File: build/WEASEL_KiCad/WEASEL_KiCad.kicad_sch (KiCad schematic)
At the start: 1 part

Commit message: Virtual Patch bay added to schematic
Virtual modular patch bay added
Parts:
- added D1, D10, D11, D12, D13, D14, D15, D16, D17, D18, D19, D2, D20, D21, D22, D23, D24, D25, D26, D27, D28, D29, D3, D4, D6, D7, D8, D9: 1N4148, DIYSynthMNL:D_4148_BigPads, symbol PCM_4ms_Diode:D_Generic
- added R1, R2, R3, R4: 10k, PCM_4ms_Resistor:R_Axial_DIN0207_L6.3mm_D2.5mm_P7.62mm_Horizontal, symbol Device:R
- added SW1: SEQ>PULSER, symbol Switch:SW_Push
- added SW10: RANDOMVOLT>MODOSC_FREQ, symbol Switch:SW_Push
- added SW11: SEQ>MODOSC_MODAMNT, symbol Switch:SW_Push
- added SW12: EG>MODOSC_MODAMNT, symbol Switch:SW_Push
- added SW13: PULSER>MODOSC_MODAMNT, symbol Switch:SW_Push
- added SW14: RANDOMVOLT>MODOSC_MODAMNT, symbol Switch:SW_Push
- added SW15: SEQ>COMPLEX_PITCH, symbol Switch:SW_Push
- added SW16: EG>COMPLEX_PITCH, symbol Switch:SW_Push
- added SW17: PULSER>COMPLEX_PITCH, symbol Switch:SW_Push
- added SW18: RANDOMVOLT>COMPLEX_PITCH, symbol Switch:SW_Push
- added SW19: SEQ>COMPLEX_TIMBRE, symbol Switch:SW_Push
- added SW2: SW_SPDT_MSM, symbol Switch:SW_SPDT_MSM
- added SW20: EG>COMPLEX_TIMBRE, symbol Switch:SW_Push
- added SW21: PULSER>COMPLEX_TIMBRE, symbol Switch:SW_Push
- added SW22: RANDOMVOLT>COMPLEX_TIMBRE, symbol Switch:SW_Push
- added SW23: SEQ>LPG_LEVEL1, symbol Switch:SW_Push
- added SW24: EG>LPG_LEVEL1, symbol Switch:SW_Push
- added SW25: PULSER>LPG_LEVEL1, symbol Switch:SW_Push
- added SW26: RANDOMVOLT>LPG_LEVEL1, symbol Switch:SW_Push
- added SW27: SEQ>LPG_LEVEL2, symbol Switch:SW_Push
- added SW28: EG>LPG_LEVEL2, symbol Switch:SW_Push
- added SW29: PULSER>LPG_LEVEL2, symbol Switch:SW_Push
- added SW3: EG>PULSER, symbol Switch:SW_Push
- added SW30: RANDOMVOLT>LPG_LEVEL2, symbol Switch:SW_Push
- added SW4: N/C, symbol Switch:SW_Push
- added SW5: RNDMVOLT>PULSER, symbol Switch:SW_Push
- added SW7: SEQ>MODOSC_FREQ, symbol Switch:SW_Push
- added SW8: EG>MODOSC_FREQ, symbol Switch:SW_Push
- added SW9: PULSER>MODOSC_FREQ, symbol Switch:SW_Push
- added U1: CD74HC4067M, Package_SO:SOIC-24W_7.5x15.4mm_P1.27mm, symbol 74xx:CD74HC4067M
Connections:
- net Vcc: now reaches A1.38 (3V3_D)
- net Vcc: now also U1.24 (VCC)
- net DGND: now reaches A1.40 (DGND)
- net DGND: now also R1.2, R2.2, R3.2, R4.2, U1.12 (GND), U1.15 (~{E})
- new net: D25.2 (A), SW26.2
- new net: D17.2 (A), SW18.2
- new net: D23.2 (A), SW24.2
- new net: D7.2 (A), SW8.2
- new net: D27.2 (A), SW28.2
- new net: D26.2 (A), SW27.2
- new net: D6.2 (A), SW7.2
- new net: D16.2 (A), SW17.2
- new net: D11.2 (A), SW12.2
- new net: D20.2 (A), SW21.2
- new net: D12.2 (A), SW13.2
- new net: D9.2 (A), SW10.2
- new net: D1.2 (A), SW1.2
- new net: D8.2 (A), SW9.2
- new net: D22.2 (A), SW23.2
- new net: D24.2 (A), SW25.2
- new net: D4.2 (A), SW5.2
- new net: D19.2 (A), SW20.2
- new net: D13.2 (A), SW14.2
- new net: D10.2 (A), SW11.2
- new net: D14.2 (A), SW15.2
- new net: D28.2 (A), SW29.2
- new net: D15.2 (A), SW16.2
- new net: D21.2 (A), SW22.2
- new net: D18.2 (A), SW19.2
- new net: D29.2 (A), SW30.2
- new net: D2.2 (A), SW3.2
- new net: D3.2 (A), SW4.2
- new net X0: R1.1, SW1.1, SW11.1, SW15.1, SW19.1, SW23.1, SW27.1, SW7.1
- new net X1: R2.1, SW12.1, SW16.1, SW20.1, SW24.1, SW28.1, SW3.1, SW8.1
- new net X2: R3.1, SW13.1, SW17.1, SW21.1, SW25.1, SW29.1, SW4.1, SW9.1
- new net X3: R4.1, SW10.1, SW14.1, SW18.1, SW22.1, SW26.1, SW30.1, SW5.1
- new net Y0: D1.1 (K), D2.1 (K), D3.1 (K), D4.1 (K)
- new net Y1: D6.1 (K), D7.1 (K), D8.1 (K), D9.1 (K)
- new net Y2: D10.1 (K), D11.1 (K), D12.1 (K), D13.1 (K)
- new net Y3: D14.1 (K), D15.1 (K), D16.1 (K), D17.1 (K)
- new net Y4: D18.1 (K), D19.1 (K), D20.1 (K), D21.1 (K)
- new net Y5: D22.1 (K), D23.1 (K), D24.1 (K), D25.1 (K)
- new net Y6: D26.1 (K), D27.1 (K), D28.1 (K), D29.1 (K)
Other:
- note added: "COMPLEX OSC PITCH_INPUT"
- note added: "COMPLEX OSC TIMBRE_INPUT"
- note added: "CONTROL SWITCHES"
- note added: "EG_OUTPUT"
- note added: "LPG LEVEL 1_INPUT"
- note added: "LPG LEVEL 2_INPUT"
- note added: "MOD OSC FREQ_INPUT"
- note added: "MOD OSC MOD AMNT_INPUT"
- note added: "PULSER PERIOD_INPUT"
- note added: "PULSER_OUTPUT"
- note added: "RANDOM VOLTAGE_OUTPUT"
- note added: "SEQUENCER"
- note added: "SEQUENCER_OUTPUT"
- note added: "VIRTUAL MODULAR MATRIX"

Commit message: Schematic and PCB Changes
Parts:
- removed D10, D11, D12, D13, D14, D15, D16, D17, D18, D19, D20, D21, D22, D23, D24, D25, D26, D27, D28, D29, D9: 1N4148, DIYSynthMNL:D_4148_BigPads, symbol PCM_4ms_Diode:D_Generic
- removed SW1: SEQ>PULSER, symbol Switch:SW_Push
- removed SW10: RANDOMVOLT>MODOSC_FREQ, symbol Switch:SW_Push
- removed SW11: SEQ>MODOSC_MODAMNT, symbol Switch:SW_Push
- removed SW12: EG>MODOSC_MODAMNT, symbol Switch:SW_Push
- removed SW13: PULSER>MODOSC_MODAMNT, symbol Switch:SW_Push
- removed SW14: RANDOMVOLT>MODOSC_MODAMNT, symbol Switch:SW_Push
- removed SW15: SEQ>COMPLEX_PITCH, symbol Switch:SW_Push
- removed SW16: EG>COMPLEX_PITCH, symbol Switch:SW_Push
- removed SW17: PULSER>COMPLEX_PITCH, symbol Switch:SW_Push
- removed SW18: RANDOMVOLT>COMPLEX_PITCH, symbol Switch:SW_Push
- removed SW19: SEQ>COMPLEX_TIMBRE, symbol Switch:SW_Push
- removed SW2: SW_SPDT_MSM, symbol Switch:SW_SPDT_MSM
- removed SW20: EG>COMPLEX_TIMBRE, symbol Switch:SW_Push
- removed SW21: PULSER>COMPLEX_TIMBRE, symbol Switch:SW_Push
- removed SW22: RANDOMVOLT>COMPLEX_TIMBRE, symbol Switch:SW_Push
- removed SW23: SEQ>LPG_LEVEL1, symbol Switch:SW_Push
- removed SW24: EG>LPG_LEVEL1, symbol Switch:SW_Push
- removed SW25: PULSER>LPG_LEVEL1, symbol Switch:SW_Push
- removed SW26: RANDOMVOLT>LPG_LEVEL1, symbol Switch:SW_Push
- removed SW27: SEQ>LPG_LEVEL2, symbol Switch:SW_Push
- removed SW28: EG>LPG_LEVEL2, symbol Switch:SW_Push
- removed SW29: PULSER>LPG_LEVEL2, symbol Switch:SW_Push
- removed SW3: EG>PULSER, symbol Switch:SW_Push
- removed SW30: RANDOMVOLT>LPG_LEVEL2, symbol Switch:SW_Push
- removed SW4: N/C, symbol Switch:SW_Push
- removed SW5: RNDMVOLT>PULSER, symbol Switch:SW_Push
- removed SW7: SEQ>MODOSC_FREQ, symbol Switch:SW_Push
- removed SW8: EG>MODOSC_FREQ, symbol Switch:SW_Push
- removed SW9: PULSER>MODOSC_FREQ, symbol Switch:SW_Push
- added C1, C10, C11, C12, C13, C14, C15, C16, C17, C18, C19, C2, C20, C21, C22, C23, C24, C25, C26, C3, C4, C5, C6, C7, C8, C9: 10nF, DIYSynthMNL:C_Rect_L7.0mm_W2.0mm_P5.00mm_BigPads, symbol Device:C
- added D30, D31, D32, D33, D34, D35, D36, D37, D38, D39, D40, D41, D42, D43, D44, D45, D46, D47, D48, D49, D5: 1N4148, DIYSynthMNL:D_4148_BigPads, symbol PCM_4ms_Diode:D_Generic
- added J1: MIDI IN, Connector_Audio:Jack_3.5mm_CUI_SJ1-3523N_Horizontal, symbol Connector_Audio:AudioJack3
- added J10: LPG_LEVEL2CTRL, Connector_Audio:Jack_3.5mm_QingPu_WQP-PJ398SM_Vertical_CircularHoles, symbol Connector_Audio:AudioJack2_SwitchT
- added J14: SEQ_OUTPUT2, Connector_Audio:Jack_3.5mm_QingPu_WQP-PJ398SM_Vertical_CircularHoles, symbol Connector_Audio:AudioJack2_SwitchT
- added J15: SEQ_OUTPUT3, Connector_Audio:Jack_3.5mm_QingPu_WQP-PJ398SM_Vertical_CircularHoles, symbol Connector_Audio:AudioJack2_SwitchT
- added J16: EG_OUTPUT1, Connector_Audio:Jack_3.5mm_QingPu_WQP-PJ398SM_Vertical_CircularHoles, symbol Connector_Audio:AudioJack2_SwitchT
- added J17: EG_OUTPUT2, Connector_Audio:Jack_3.5mm_QingPu_WQP-PJ398SM_Vertical_CircularHoles, symbol Connector_Audio:AudioJack2_SwitchT
- added J18: EG_OUTPUT3, Connector_Audio:Jack_3.5mm_QingPu_WQP-PJ398SM_Vertical_CircularHoles, symbol Connector_Audio:AudioJack2_SwitchT
- added J19: PLSR_OUTPUT1, Connector_Audio:Jack_3.5mm_QingPu_WQP-PJ398SM_Vertical_CircularHoles, symbol Connector_Audio:AudioJack2_SwitchT
- added J2: STEREO_OUTPUT, Connector_Audio:Jack_3.5mm_CUI_SJ1-3523N_Horizontal, symbol Connector_Audio:AudioJack3
- added J20: PLSR_OUTPUT2, Connector_Audio:Jack_3.5mm_QingPu_WQP-PJ398SM_Vertical_CircularHoles, symbol Connector_Audio:AudioJack2_SwitchT
- added J21: PLSR_OUTPUT3, Connector_Audio:Jack_3.5mm_QingPu_WQP-PJ398SM_Vertical_CircularHoles, symbol Connector_Audio:AudioJack2_SwitchT
- added J22: RNDM_OUTPUT1, Connector_Audio:Jack_3.5mm_QingPu_WQP-PJ398SM_Vertical_CircularHoles, symbol Connector_Audio:AudioJack2_SwitchT
- added J23: RNDM_OUTPUT2, Connector_Audio:Jack_3.5mm_QingPu_WQP-PJ398SM_Vertical_CircularHoles, symbol Connector_Audio:AudioJack2_SwitchT
- added J24: RNDM_OUTPUT3, Connector_Audio:Jack_3.5mm_QingPu_WQP-PJ398SM_Vertical_CircularHoles, symbol Connector_Audio:AudioJack2_SwitchT
- added J3: SEQ_OUTPUT1, Connector_Audio:Jack_3.5mm_QingPu_WQP-PJ398SM_Vertical_CircularHoles, symbol Connector_Audio:AudioJack2_SwitchT
- added J4: PLSR_PERIODCTRL, Connector_Audio:Jack_3.5mm_QingPu_WQP-PJ398SM_Vertical_CircularHoles, symbol Connector_Audio:AudioJack2_SwitchT
- added J5: MODOSC_FREQCTRL, Connector_Audio:Jack_3.5mm_QingPu_WQP-PJ398SM_Vertical_CircularHoles, symbol Connector_Audio:AudioJack2_SwitchT
- added J6: MODOSC_MODCTRL, Connector_Audio:Jack_3.5mm_QingPu_WQP-PJ398SM_Vertical_CircularHoles, symbol Connector_Audio:AudioJack2_SwitchT
- added J7: COMPOSC_PITCHCTRL, Connector_Audio:Jack_3.5mm_QingPu_WQP-PJ398SM_Vertical_CircularHoles, symbol Connector_Audio:AudioJack2_SwitchT
- added J8: COMPOSC_WAVEFOLDERCTRL, Connector_Audio:Jack_3.5mm_QingPu_WQP-PJ398SM_Vertical_CircularHoles, symbol Connector_Audio:AudioJack2_SwitchT
- added J9: LPG_LEVEL1CTRL, Connector_Audio:Jack_3.5mm_QingPu_WQP-PJ398SM_Vertical_CircularHoles, symbol Connector_Audio:AudioJack2_SwitchT
- added R10, R9: 220R, PCM_4ms_Resistor:R_Axial_DIN0207_L6.3mm_D2.5mm_P7.62mm_Horizontal, symbol Device:R
- added R5, R6, R7, R8: 10k, PCM_4ms_Resistor:R_Axial_DIN0207_L6.3mm_D2.5mm_P7.62mm_Horizontal, symbol Device:R
- added RV1: SQ_Step1, DIYSynthMNL:Potentiometer_RV09_BigPads, symbol Device:R_Potentiometer
- added RV10: PLSR_PERIOD, DIYSynthMNL:Potentiometer_RV09_BigPads, symbol Device:R_Potentiometer
- added RV11: MODOSC_FREQCTRL, DIYSynthMNL:Potentiometer_RV09_BigPads, symbol Device:R_Potentiometer
- added RV12: MODOSC_FREQ, DIYSynthMNL:Potentiometer_RV09_BigPads, symbol Device:R_Potentiometer
- added RV13: MODOSC_MODULATIONCTRL, DIYSynthMNL:Potentiometer_RV09_BigPads, symbol Device:R_Potentiometer
- added RV14: MODOSC_MODULATION, DIYSynthMNL:Potentiometer_RV09_BigPads, symbol Device:R_Potentiometer
- added RV15: MODOSC_FINE, DIYSynthMNL:Potentiometer_RV09_BigPads, symbol Device:R_Potentiometer
- added RV16: COMPLEXOSC_FREQCTRL, DIYSynthMNL:Potentiometer_RV09_BigPads, symbol Device:R_Potentiometer
- added RV17: COMPLEXOSC_FREQ, DIYSynthMNL:Potentiometer_RV09_BigPads, symbol Device:R_Potentiometer
- added RV18: COMPLEXOSC_FINE, DIYSynthMNL:Potentiometer_RV09_BigPads, symbol Device:R_Potentiometer
- added RV19: COMPLEXOSC_WAVEFOLDERCTRL, DIYSynthMNL:Potentiometer_RV09_BigPads, symbol Device:R_Potentiometer
- added RV2: SQ_Step2, DIYSynthMNL:Potentiometer_RV09_BigPads, symbol Device:R_Potentiometer
- added RV20: COMPLEXOSC_WAVEFOLDER, DIYSynthMNL:Potentiometer_RV09_BigPads, symbol Device:R_Potentiometer
- added RV21: COMPLEXOSC_TIMBRE, DIYSynthMNL:Potentiometer_RV09_BigPads, symbol Device:R_Potentiometer
- added RV22: LPG_LEVEL1CTRL, DIYSynthMNL:Potentiometer_RV09_BigPads, symbol Device:R_Potentiometer
- added RV23: LPG_LEVEL1, DIYSynthMNL:Potentiometer_RV09_BigPads, symbol Device:R_Potentiometer
- added RV24: LPG_LEVEL2CTRL, DIYSynthMNL:Potentiometer_RV09_BigPads, symbol Device:R_Potentiometer
- added RV25: LPG_LEVEL2, DIYSynthMNL:Potentiometer_RV09_BigPads, symbol Device:R_Potentiometer
- added RV26: CLOCK, DIYSynthMNL:Potentiometer_RV09_BigPads, symbol Device:R_Potentiometer
- added RV3: SQ_Step3, DIYSynthMNL:Potentiometer_RV09_BigPads, symbol Device:R_Potentiometer
- added RV4: SQ_Step4, DIYSynthMNL:Potentiometer_RV09_BigPads, symbol Device:R_Potentiometer
- added RV5: SQ_Step5, DIYSynthMNL:Potentiometer_RV09_BigPads, symbol Device:R_Potentiometer
- added RV6: EG_ATTACK, DIYSynthMNL:Potentiometer_RV09_BigPads, symbol Device:R_Potentiometer
- added RV7: EG_SUSTAIN, DIYSynthMNL:Potentiometer_RV09_BigPads, symbol Device:R_Potentiometer
- added RV8: EG_DECAY, DIYSynthMNL:Potentiometer_RV09_BigPads, symbol Device:R_Potentiometer
- added RV9: PLSR_PERIODCTRL, DIYSynthMNL:Potentiometer_RV09_BigPads, symbol Device:R_Potentiometer
- added SW1: SQ_TOGGLESTEP1, DIYSynthMNL:ToggleSwitch_MTS-102_SPDT, symbol Switch:SW_SPDT
- added SW2: SEQ_TRIGGERSELECT, PCM_4ms_Experimental_FP:SW_PUSH_6mm_H13mm, symbol Switch:SW_Push
- added SW3: SQ_TOGGLESTEP2, DIYSynthMNL:ToggleSwitch_MTS-102_SPDT, symbol Switch:SW_SPDT
- added SW31: EG_TRIGGERSELECT, PCM_4ms_Experimental_FP:SW_PUSH_6mm_H13mm, symbol Switch:SW_Push
- added SW32: EG_MODESELECT, PCM_4ms_Experimental_FP:SW_PUSH_6mm_H13mm, symbol Switch:SW_Push
- added SW33: PLSR_TRIGGERSELECT, PCM_4ms_Experimental_FP:SW_PUSH_6mm_H13mm, symbol Switch:SW_Push
- added SW34: PLSR_MODE, PCM_4ms_Experimental_FP:SW_PUSH_6mm_H13mm, symbol Switch:SW_Push
- added SW35: MODOSC_MIDITOGGLE, PCM_4ms_Experimental_FP:SW_PUSH_6mm_H13mm, symbol Switch:SW_Push
- added SW36: MODOSC_PITCHTRANGE, PCM_4ms_Experimental_FP:SW_PUSH_6mm_H13mm, symbol Switch:SW_Push
- added SW37: COMPLEXOSC_MIDITOGGLE, PCM_4ms_Experimental_FP:SW_PUSH_6mm_H13mm, symbol Switch:SW_Push
- added SW38: COMPLEXOSC_POLARITY, PCM_4ms_Experimental_FP:SW_PUSH_6mm_H13mm, symbol Switch:SW_Push
- added SW39: COMPLEXOSC_WAVETOGGLE, PCM_4ms_Experimental_FP:SW_PUSH_6mm_H13mm, symbol Switch:SW_Push
- added SW4: SQ_TOGGLESTEP3, DIYSynthMNL:ToggleSwitch_MTS-102_SPDT, symbol Switch:SW_SPDT
- added SW40: LPG_GATE1MODE, PCM_4ms_Experimental_FP:SW_PUSH_6mm_H13mm, symbol Switch:SW_Push
- added SW41: LPG_GATE2MODE, PCM_4ms_Experimental_FP:SW_PUSH_6mm_H13mm, symbol Switch:SW_Push
- added SW42: RNDMVOLTAGE_TRIGGERSELECT, PCM_4ms_Experimental_FP:SW_PUSH_6mm_H13mm, symbol Switch:SW_Push
- added SW43: CLOCK_SYNCTOGGLE, PCM_4ms_Experimental_FP:SW_PUSH_6mm_H13mm, symbol Switch:SW_Push
- added SW5: SQ_TOGGLESTEP4, DIYSynthMNL:ToggleSwitch_MTS-102_SPDT, symbol Switch:SW_SPDT
- added SW6: SEQ_STAGES, PCM_4ms_Experimental_FP:SW_PUSH_6mm_H13mm, symbol Switch:SW_Push
- added SW7: SQ_TOGGLESTEP5, DIYSynthMNL:ToggleSwitch_MTS-102_SPDT, symbol Switch:SW_SPDT
- added U2: CD74HC4067M, Package_SO:SOIC-24W_7.5x15.4mm_P1.27mm, symbol 74xx:CD74HC4067M
- added U3: 6N138, DIYSynthMNL:DIP-8_W7.62mm_LongPads, symbol Isolator:6N138
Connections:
- net DGND: now also U2.15 (~{E}); no longer A1.40 (DGND), R1.2, R2.2, R3.2, R4.2, U1.12 (GND)
- net Vcc: now also R9.1, RV1.3, RV10.3, RV11.3, RV12.3, RV13.3, RV14.3, RV15.3, RV16.3, RV17.3, RV18.3, RV19.3, RV2.3, RV20.3, RV21.3, RV22.3, RV23.3, RV24.3, RV25.3, RV26.3, RV3.3, RV4.3, RV5.3, RV6.3, RV7.3, RV8.3, RV9.3, U2.24 (VCC), U3.8 (VCC)
- net X0: now also A1.13 (I2C1_SDA), SW2.1, SW3.2 (B), SW33.1, SW37.1, SW41.1
- net X1: now also A1.14 (USART1_TX), SW34.1, SW38.1, SW4.2 (B), SW42.1, SW6.1
- net X2: now also A1.24 (ADC_2), SW31.1, SW35.1, SW39.1, SW43.1, SW5.2 (B)
- net X3: now also A1.25 (ADC_3), SW1.2 (B), SW32.1, SW36.1, SW40.1, SW7.2 (B)
- net Y0: now also A1.9 (SPI1_SCK), D30.1 (K), D31.1 (K), D32.1 (K), D5.1 (K); no longer D1.1 (K), D2.1 (K), D3.1 (K), D4.1 (K)
- net Y1: now also A1.10 (SPI1_POCI), D33.1 (K), D34.1 (K), D35.1 (K), D36.1 (K); no longer D6.1 (K), D7.1 (K), D8.1 (K)
- net Y2: now also A1.11 (SPI1_PICO), D37.1 (K), D38.1 (K), D39.1 (K), D40.1 (K)
- net Y3: now also A1.12 (I2C1_SCL), D41.1 (K), D42.1 (K), D43.1 (K), D45.1 (K)
- net Y4: now also A1.15 (USART1_RX), D46.1 (K), D47.1 (K), D48.1 (K), D49.1 (K)
- net at D7.2 (A): now also J9.S, J9.T, J9.TN
- net at D6.2 (A): now also J8.S, J8.T, J8.TN
- net at D1.2 (A): now also J4.S, J4.T, J4.TN
- net MUX1_S0: now reaches A1.1 (USB_ID)
- net MUX1_S0: now also U1.10 (S0)
- net OUT_L: now reaches A1.18 (AUDIO_OUT_1)
- net OUT_L: now also J2.T
- net OUT_R: now reaches A1.19 (AUDIO_OUT_2)
- net OUT_R: now also J2.R
- net MUX1_S1: now reaches A1.2 (SD_DATA_3)
- net MUX1_S1: now also U1.11 (S1)
- net GND: now reaches A1.20 (AGND)
- net GND: now also A1.40 (DGND), R1.2, R2.2, R3.2, R4.2, U1.12 (GND), C1.2, C10.2, C11.2, C12.2, C13.2, C14.2, C15.2, C16.2, C17.2, C18.2, C19.2, C2.2, C20.2, C21.2, C22.2, C23.2, C24.2, C25.2, C26.2, C3.2, C4.2, C5.2, C6.2, C7.2, C8.2, C9.2, J1.S, J2.S, R5.2, R6.2, R7.2, R8.2, RV1.1, RV10.1, RV11.1, RV12.1, RV13.1, RV14.1, RV15.1, RV16.1, RV17.1, RV18.1, RV19.1, RV2.1, RV20.1, RV21.1, RV22.1, RV23.1, RV24.1, RV25.1, RV26.1, RV3.1, RV4.1, RV5.1, RV6.1, RV7.1, RV8.1, RV9.1, U2.12 (GND), U3.5 (GND)
- net MUX1_SIGNAL: now reaches A1.22 (ADC_0)
- net MUX1_SIGNAL: now also U1.1 (COM)
- net MUX2_SIGNAL: now reaches A1.23 (ADC_1)
- net MUX2_SIGNAL: now also U2.1 (COM)
- net B0: now reaches A1.26 (ADC_4)
- net B0: now also J14.S, J14.T, J14.TN, J15.S, J15.T, J15.TN, J3.S, J3.T, J3.TN, R5.1
- net B1: now reaches A1.27 (ADC_5)
- net B1: now also J16.S, J16.T, J16.TN, J17.S, J17.T, J17.TN, J18.S, J18.T, J18.TN, R6.1
- net B2: now reaches A1.28 (ADC_6)
- net B2: now also J19.S, J19.T, J19.TN, J20.S, J20.T, J20.TN, J21.S, J21.T, J21.TN, R7.1
- net B3: now reaches A1.29 (DAC_OUT2)
- net B3: now also J22.S, J22.T, J22.TN, J23.S, J23.T, J23.TN, J24.S, J24.T, J24.TN, R8.1
- net MUX1_S2: now reaches A1.3 (SD_DATA_2)
- net MUX1_S2: now also U1.14 (S2)
- net A0: now reaches A1.30 (DAC_OUT1)
- net A0: now also D1.1 (K)
- net A1: now reaches A1.31 (SAI2_MCLK)
- net A1: now also D2.1 (K)
- net A2: now reaches A1.32 (SAI2_SD_B)
- net A2: now also D3.1 (K)
- net A3: now reaches A1.33 (SAI2_SD_A)
- net A4: now reaches A1.34 (SAI2_FS)
- net A4: now also D6.1 (K)
- net A5: now reaches A1.35 (SAI2_SCK)
- net A5: now also D7.1 (K)
- net A6: now reaches A1.36 (USB_D_-)
- net MIDI_INPUT: now reaches A1.37 (USB_D_+)
- net MIDI_INPUT: now also R9.2, U3.6 (VO2)
- net MUX1_S3: now reaches A1.4 (SD_DATA_1)
- net MUX1_S3: now also U1.13 (S3)
- net MUX2_S0: now reaches A1.5 (SD_DATA_0)
- net MUX2_S0: now also U2.10 (S0)
- net MUX2_S1: now reaches A1.6 (SD_CMD)
- net MUX2_S1: now also U2.11 (S1)
- net MUX2_S2: now reaches A1.7 (SD_CLK)
- net MUX2_S2: now also U2.14 (S2)
- net MUX2_S3: now reaches A1.8 (SPI1_CS)
- net MUX2_S3: now also U2.13 (S3)
- net at D2.2 (A): now also J5.S, J5.T, J5.TN
- net at D3.2 (A): now also J6.S, J6.T, J6.TN
- net at U1.16 (I15): now also C16.1, RV16.2
- net at U1.17 (I14): now also C14.1, RV14.2
- net at U1.18 (I13): now also C13.1, RV13.2
- net at U1.19 (I12): now also C15.1, RV15.2
- net at U1.2 (I7): now also C8.1, RV8.2
- net at U1.20 (I11): now also C12.1, RV12.2
- net at U1.21 (I10): now also C11.1, RV11.2
- net at U1.22 (I9): now also C10.1, RV10.2
- net at U1.23 (I8): now also C9.1, RV9.2
- net at U1.3 (I6): now also C7.1, RV7.2
- net at U1.4 (I5): now also C6.1, RV6.2
- net at U1.5 (I4): now also C5.1, RV5.2
- net at U1.6 (I3): now also C4.1, RV4.2
- net at U1.7 (I2): now also C3.1, RV3.2
- net at U1.8 (I1): now also C2.1, RV2.2
- net at U1.9 (I0): now also C1.1, RV1.2
- new net: D38.2 (A), SW38.2
- new net: D39.2 (A), SW39.2
- new net: D34.2 (A), SW34.2
- new net: C24.1, RV24.2, U2.2 (I7)
- new net: D49.2 (A), SW7.1 (A)
- new net: C23.1, RV23.2, U2.3 (I6)
- new net: C19.1, RV19.2, U2.7 (I2)
- new net: D41.2 (A), SW41.2
- new net: C26.1, RV26.2, U2.22 (I9)
- new net: C25.1, RV25.2, U2.23 (I8)
- new net: C22.1, RV22.2, U2.4 (I5)
- new net: C21.1, RV21.2, U2.5 (I4)
- new net: C20.1, RV20.2, U2.6 (I3)
- new net: C18.1, RV18.2, U2.8 (I1)
- new net: C17.1, RV17.2, U2.9 (I0)
- new net: D5.2 (A), SW2.2
- new net: D44.1 (K), R10.2, U3.2 (C1)
- new net: D44.2 (A), J1.T, U3.3 (C2)
- new net: D48.2 (A), SW5.1 (A)
- new net: D30.2 (A), SW6.2
- new net: D37.2 (A), SW37.2
- new net: D42.2 (A), SW42.2
- new net: D35.2 (A), SW35.2
- new net: J1.R, R10.1
- new net: D40.2 (A), SW40.2
- new net: J7.S, J7.T, J7.TN
- new net: D45.2 (A), SW1.1 (A)
- new net: J10.S, J10.T, J10.TN
- new net: D36.2 (A), SW36.2
- new net: D32.2 (A), SW32.2
- new net: D46.2 (A), SW3.1 (A)
- new net: D33.2 (A), SW33.2
- new net: D47.2 (A), SW4.1 (A)
- new net: D43.2 (A), SW43.2
- new net: D31.2 (A), SW31.2
- no-connect marks 0 -> 3
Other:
- note added: "BUTTON CONTROL MATRIX"
- note added: "COMPOSC_PITCHCTRL"
- note added: "COMPOSC_WAVEFOLDERCTRL"
- note added: "DAISY SEED"
- note added: "LINE OUTPUT"
- note added: "LPG_LEVEL1CTRL"
- note added: "LPG_LEVEL2CTRL"
- note added: "MIDI INPUT CIRCUIT"
- note added: "MODOSC_FREQCTRL"
- note added: "MODOSC_MODCTROL"
- note added: "MUX_1"
- note added: "MUX_2"
- note added: "PLSR_OUTPUT"
- note added: "PLSR_PERIODCTRL"
- note added: "RNDM_OUTPUT"
- note added: "SEQ_OUTPUT"
- note removed: "COMPLEX OSC PITCH_INPUT"
- note removed: "COMPLEX OSC TIMBRE_INPUT"
- note removed: "CONTROL SWITCHES"
- note removed: "LPG LEVEL 1_INPUT"
- note removed: "LPG LEVEL 2_INPUT"
- note removed: "MOD OSC FREQ_INPUT"
- note removed: "MOD OSC MOD AMNT_INPUT"
- note removed: "PULSER PERIOD_INPUT"
- note removed: "PULSER_OUTPUT"
- note removed: "RANDOM VOLTAGE_OUTPUT"
- note removed: "SEQUENCER"
- note removed: "SEQUENCER_OUTPUT"
- company: (none) -> .axs instruments
- title: (none) -> WEASEL | Digital West Coast Synth
- moved on the sheet: A1, R1, R2, R3, R4, U1

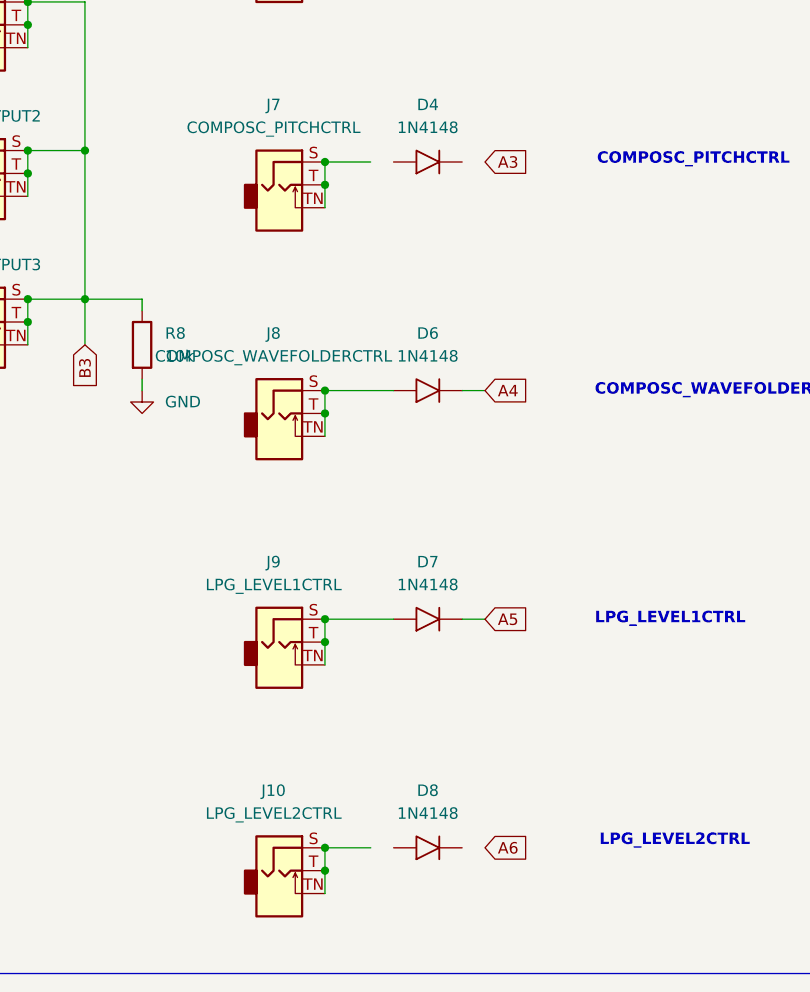
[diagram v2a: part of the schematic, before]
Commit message: pcb update
update based on schematic changes
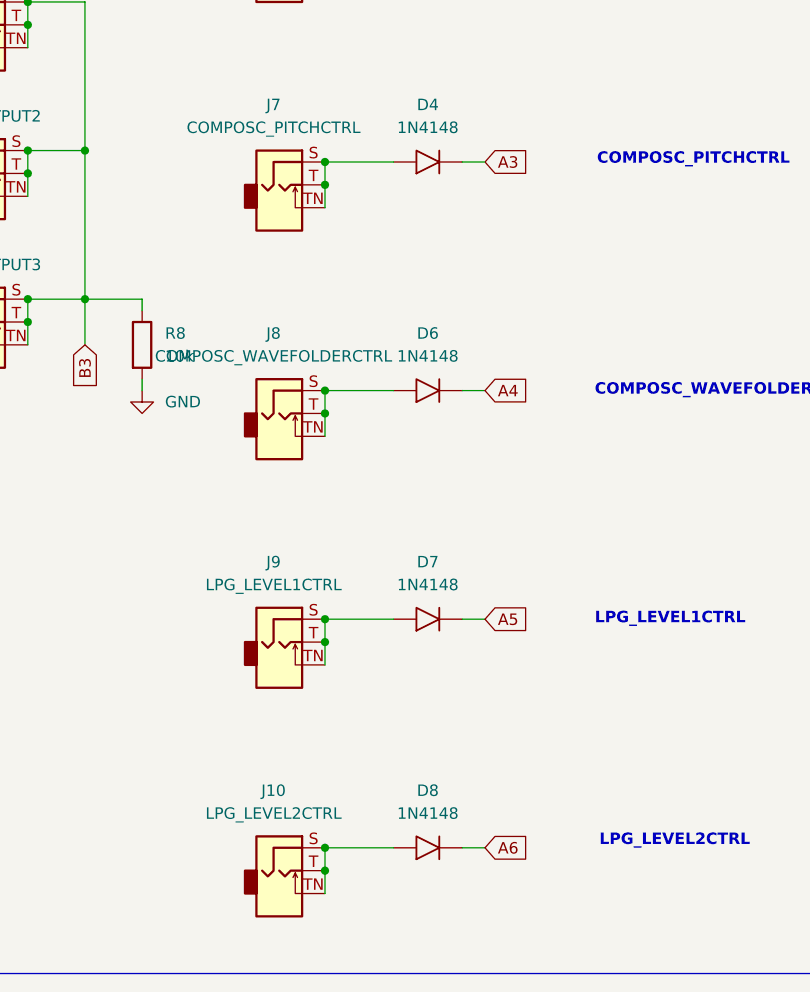
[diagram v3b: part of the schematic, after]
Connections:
- net A3: now also D4.1 (K)
- net A6: now also D8.1 (K)
- net at J7.S, J7.T, J7.TN: now also D4.2 (A)
- net at J10.S, J10.T, J10.TN: now also D8.2 (A)
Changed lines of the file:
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@@
 	(wire
 		(pts
-			(xy 443.23 292.1) (xy 438.15 292.1)
+			(xy 438.15 292.1) (xy 445.77 292.1)
 		)
 		(stroke
@@
 	(wire
 		(pts
+			(xy 453.39 368.3) (xy 455.93 368.3)
+		)
+		(stroke
+			(width 0)
+			(type default)
+		)
+	)
+	(wire
+		(pts
 			(xy 276.86 234.95) (xy 276.86 241.3)
 		)
@@
 	(wire
 		(pts
+			(xy 453.39 292.1) (xy 455.93 292.1)
+		)
+		(stroke
+			(width 0)
+			(type default)
+		)
+	)
+	(wire
+		(pts
 			(xy 292.1 307.34) (xy 297.18 307.34)
 		)
@@
 	(wire
 		(pts
-			(xy 443.23 368.3) (xy 438.15 368.3)
-		)
-		(stroke
+			(xy 438.15 368.3) (xy 445.77 368.3)
+		)
+		(stroke

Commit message: Update Schematic
- changed MUX to module instead of SMD IC
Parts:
- removed U1, U2: CD74HC4067M, Package_SO:SOIC-24W_7.5x15.4mm_P1.27mm, symbol 74xx:CD74HC4067M
- added C27: 10nF, DIYSynthMNL:C_Rect_L7.0mm_W2.0mm_P5.00mm_BigPads, symbol Device:C
- added RV27: REVERB_MIX, DIYSynthMNL:Potentiometer_RV09_BigPads, symbol Device:R_Potentiometer
- added U1, U2: CD74HC4067, MODULE, symbol CD74HC4067:CD74HC4067
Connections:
- net GND: now also C27.2, RV27.1, U1.12 (gnd), U1.15 (e), U2.12 (gnd), U2.15 (e)
- net MUX1_S0: now also U1.10 (s0)
- net MUX1_S1: now also U1.11 (s1)
- net MUX1_S2: now also U1.14 (s2)
- net MUX1_S3: now also U1.13 (s3)
- net MUX1_SIGNAL: now also U1.1 (vout)
- net MUX2_S0: now also U2.10 (s0)
- net MUX2_S1: now also U2.11 (s1)
- net MUX2_S2: now also U2.14 (s2)
- net MUX2_S3: now also U2.13 (s3)
- net MUX2_SIGNAL: now also U2.1 (vout)
- net Vcc: now also RV27.3, U1.24 (vcc), U2.24 (vcc)
- net at C9.1, RV9.2: now also U1.23 (i8)
- net at C15.1, RV15.2: now also U1.19 (i12)
- net at C3.1, RV3.2: now also U1.7 (i2)
- net at C24.1, RV24.2: now also U2.2 (i7)
- net at C23.1, RV23.2: now also U2.3 (i6)
- net at C19.1, RV19.2: now also U2.7 (i2)
- net at C12.1, RV12.2: now also U1.20 (i11)
- net at C26.1, RV26.2: now also U2.22 (i9)
- net at C25.1, RV25.2: now also U2.23 (i8)
- net at C22.1, RV22.2: now also U2.4 (i5)
- net at C21.1, RV21.2: now also U2.5 (i4)
- net at C20.1, RV20.2: now also U2.6 (i3)
- net at C18.1, RV18.2: now also U2.8 (i1)
- net at C17.1, RV17.2: now also U2.9 (i0)
- net at C11.1, RV11.2: now also U1.21 (i10)
- net at C14.1, RV14.2: now also U1.17 (i14)
- net at C6.1, RV6.2: now also U1.4 (i5)
- net at C5.1, RV5.2: now also U1.5 (i4)
- net at C8.1, RV8.2: now also U1.2 (i7)
- net at C10.1, RV10.2: now also U1.22 (i9)
- net at C1.1, RV1.2: now also U1.9 (i0)
- net at C2.1, RV2.2: now also U1.8 (i1)
- net at C7.1, RV7.2: now also U1.3 (i6)
- net at C4.1, RV4.2: now also U1.6 (i3)
- net at C16.1, RV16.2: now also U1.16 (i15)
- net at C13.1, RV13.2: now also U1.18 (i13)
- new net: C27.1, RV27.2, U2.21 (i10)
- no-connect marks 3 -> 9
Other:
- moved on the sheet: A1, C1, C10, C11, C12, C13, C14, C15, C16, C17, C18, C19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

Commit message: Schematic and PCB Update
- PCB changes
-
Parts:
- U1, U2: footprint MODULE -> CD74HC4067 MUX:CD74HC4067
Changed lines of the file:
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@@
 			)
 		)
-		(property "Footprint" "MODULE"
+		(property "Footprint" "CD74HC4067 MUX:CD74HC4067"
 			(at 278.13 104.14 0)
 			(effects
@@
 			)
 		)
-		(property "Footprint" "MODULE"
+		(property "Footprint" "CD74HC4067 MUX:CD74HC4067"
 			(at 341.63 234.95 0)
 			(effects

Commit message: PCB Layout v1.0
- Finished PCB Layout v1.0
- Gerbers generated
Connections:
- net GND: now also RV12.3; no longer RV12.1
- net Vcc: now also RV12.1; no longer RV12.3
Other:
- moved on the sheet: RV12
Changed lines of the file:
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@@
 	(symbol
 		(lib_id "Device:R_Potentiometer")
-		(at 604.52 54.61 270)
+		(at 604.52 54.61 90)
+		(mirror x)
 		(unit 1)
 		(exclude_from_sim no)
@@
 		(on_board yes)
 		(dnp no)
-		(fields_autoplaced yes)
 		(property "Reference" "RV12"
 			(at 604.52 48.26 90)
